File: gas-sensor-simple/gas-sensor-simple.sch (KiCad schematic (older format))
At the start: 43 parts, among them J1 RPi, J2 digital header, J3 digital header, J4 1x2, J5 1x2, J6 1x2, J7 1x2, U1 MQ-8, U10 RG LED, U12 LM393, U13 ads1x15, U14 ads1x15, U15 BME280, U2 MQ-4, U3 DFRobotCO2, U4 O2, U5 7407, U6 7407, U7 RG LED, U8 RG LED, U9 RG LED

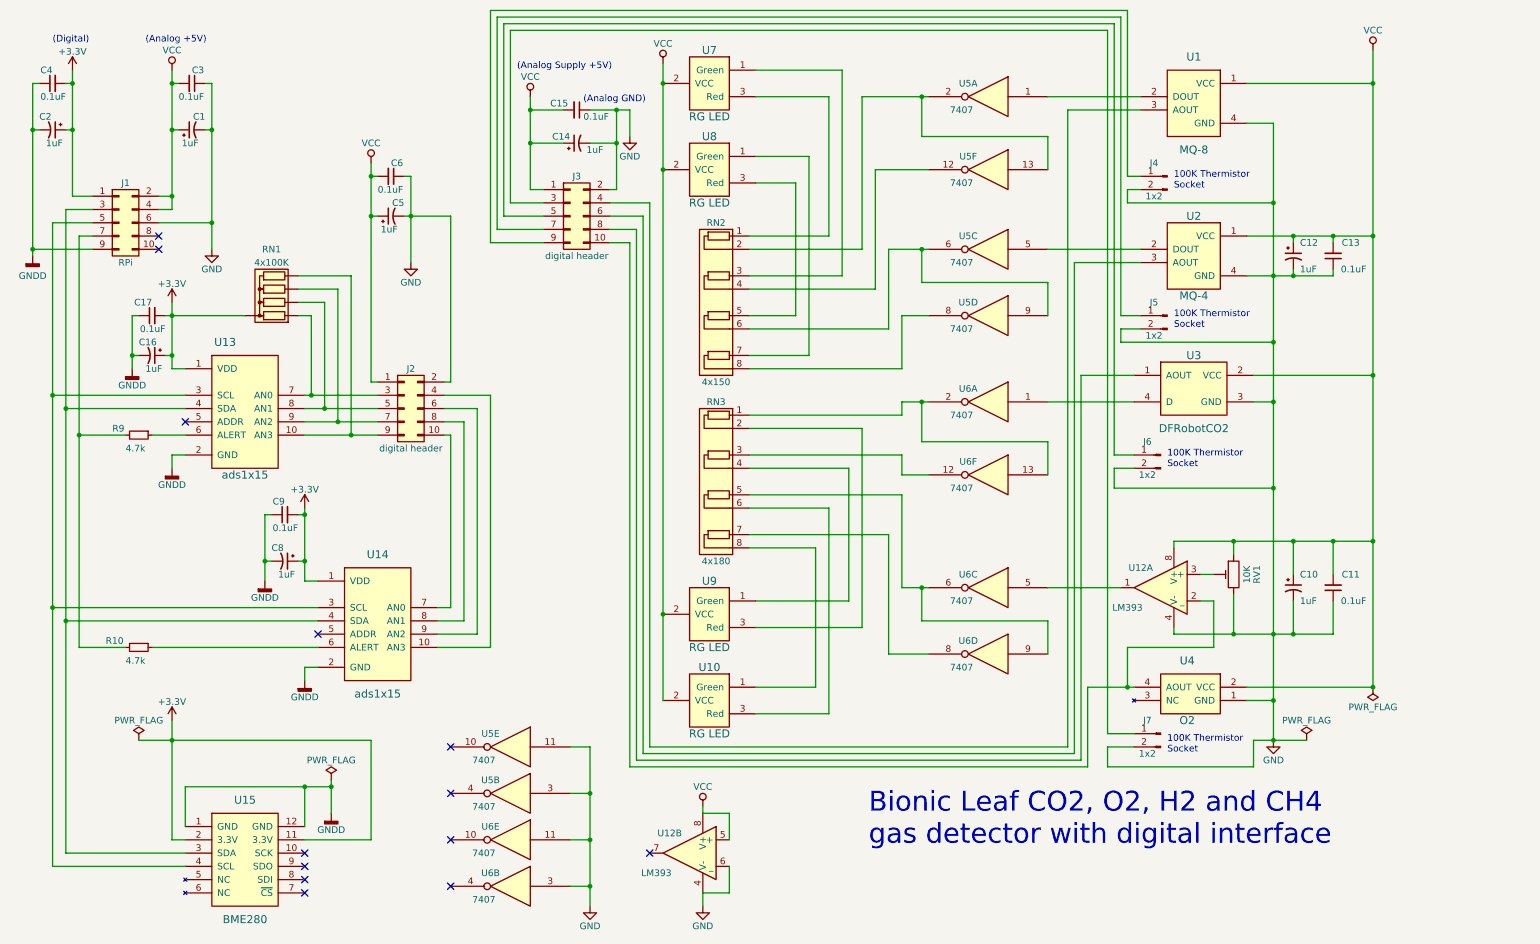
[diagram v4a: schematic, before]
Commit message: Add ground planes. Create new gerbers in layout2.gerbers.
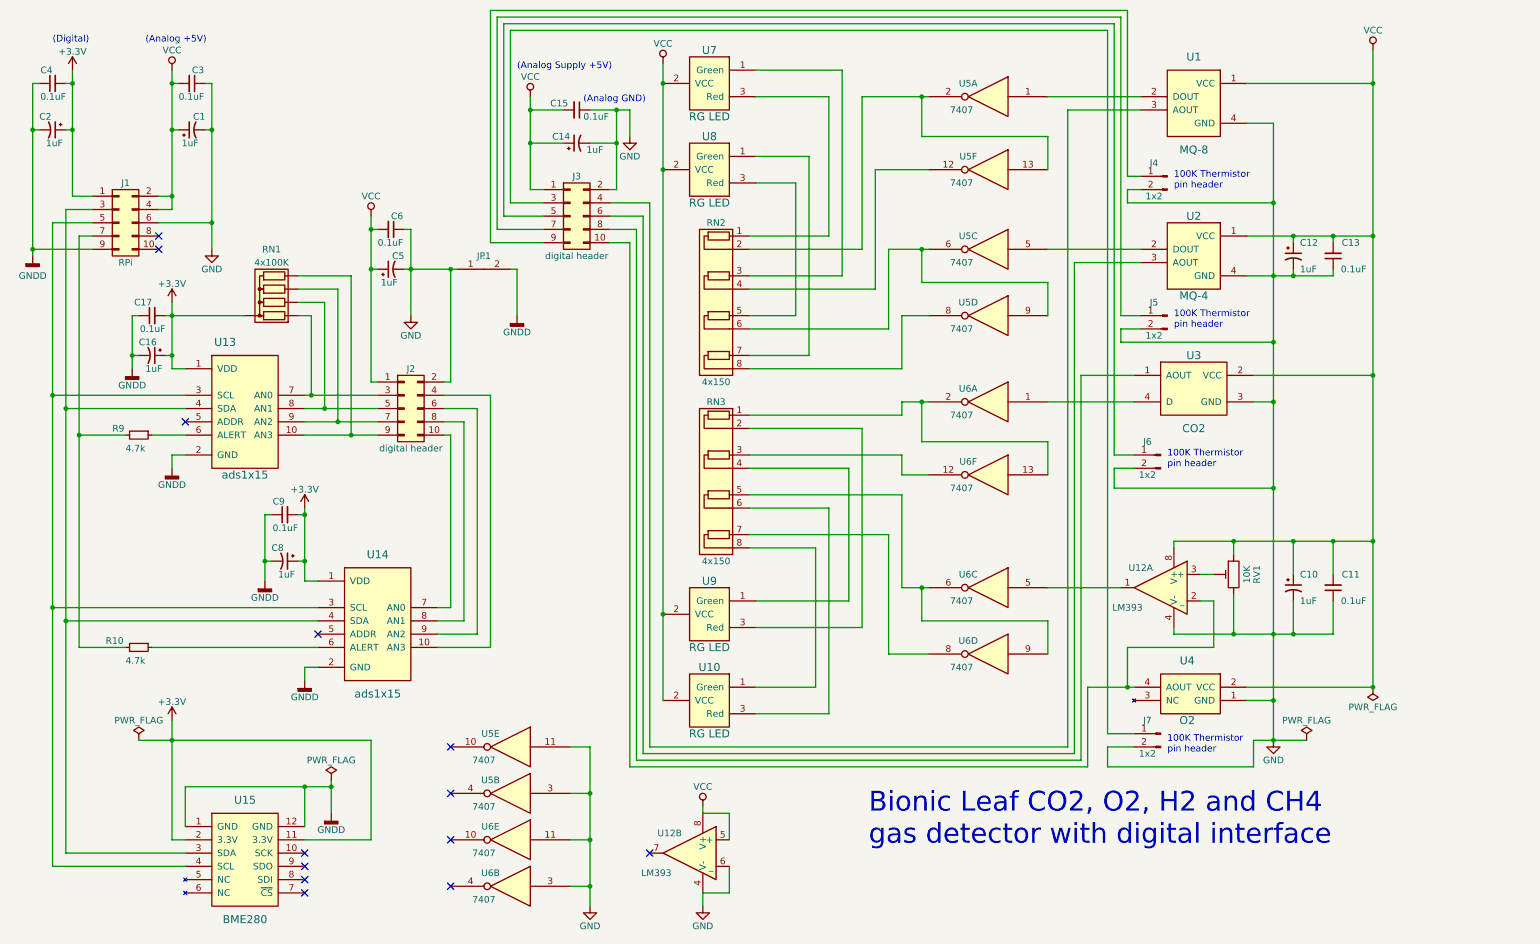
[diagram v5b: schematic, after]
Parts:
- added JP1: ., Resistors_SMD:R_0402_NoSilk, symbol pavillion
- RN3: value 4x180 -> 4x150
- U3: value DFRobotCO2 -> CO2
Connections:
- net GND: now also JP1.1
- net GNDD: now also JP1.2
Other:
- note added: "100K Thermistor\npin header"
- note removed: "100K Thermistor\nSocket"
- moved on the sheet: C5, C6
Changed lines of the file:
@@
 P 9500 3600
 F 0 "U3" H 9500 3850 60  0000 C CNN
-F 1 "DFRobotCO2" H 9500 3300 60  0000 C CNN
+F 1 "CO2" H 9500 3300 60  0000 C CNN
 F 2 "Socket_Strips:Socket_Strip_Straight_1x04_Pitch2.54mm" H 9500 3300 60  0001 C CNN
 F 3 "" H 9500 3300 60  0001 C CNN
@@
 L GND #PWR015
 U 1 1 5A065453
-P 3600 2650
-F 0 "#PWR015" H 3600 2400 50  0001 C CNN
-F 1 "GND" H 3600 2500 50  0000 C CNN
-F 2 "" H 3600 2650 50  0001 C CNN
-F 3 "" H 3600 2650 50  0001 C CNN
-	1    3600 2650
+P 3600 3050
+F 0 "#PWR015" H 3600 2800 50  0001 C CNN
+F 1 "GND" H 3600 2900 50  0000 C CNN
+F 2 "" H 3600 3050 50  0001 C CNN
+F 3 "" H 3600 3050 50  0001 C CNN
+	1    3600 3050
 	1    0    0    -1
 $EndComp
@@
 L VCC #PWR016
 U 1 1 5A024ADB
-P 3300 1900
-F 0 "#PWR016" H 3300 1750 50  0001 C CNN
-F 1 "VCC" H 3300 2050 50  0000 C CNN
-F 2 "" H 3300 1900 50  0001 C CNN
-F 3 "" H 3300 1900 50  0001 C CNN
-	1    3300 1900
+P 3300 2300
+F 0 "#PWR016" H 3300 2150 50  0001 C CNN
+F 1 "VCC" H 3300 2450 50  0000 C CNN
+F 2 "" H 3300 2300 50  0001 C CNN
+F 3 "" H 3300 2300 50  0001 C CNN
+	1    3300 2300
 	1    0    0    -1
 $EndComp
@@
 L CP1_Small C5
 U 1 1 5A0B3058
-P 3450 2300
-F 0 "C5" V 3550 2200 50  0000 L CNN
-F 1 "1uF" V 3350 2250 50  0000 L CNN
-F 2 "Capacitors_THT:CP_Radial_D5.0mm_P2.00mm" H 3450 2300 50  0001 C CNN
-F 3 "" H 3450 2300 50  0001 C CNN
-	1    3450 2300
+P 3450 2700
+F 0 "C5" V 3550 2600 50  0000 L CNN
+F 1 "1uF" V 3350 2650 50  0000 L CNN
+F 2 "Capacitors_THT:CP_Radial_D5.0mm_P2.00mm" H 3450 2700 50  0001 C CNN
+F 3 "" H 3450 2700 50  0001 C CNN
+	1    3450 2700
 	0    -1   -1   0
 $EndComp
@@
 L C_Small C6
 U 1 1 5A0B305E
-P 3450 2000
-F 0 "C6" V 3350 2000 50  0000 L CNN
-F 1 "0.1uF" V 3550 1900 50  0000 L CNN
-F 2 "Capacitors_THT:C_Disc_D5.0mm_W2.5mm_P2.50mm" H 3450 2000 50  0001 C CNN
-F 3 "" H 3450 2000 50  0001 C CNN
-	1    3450 2000
+P 3450 2400
+F 0 "C6" V 3350 2400 50  0000 L CNN
+F 1 "0.1uF" V 3550 2300 50  0000 L CNN
+F 2 "Capacitors_THT:C_Disc_D5.0mm_W2.5mm_P2.50mm" H 3450 2400 50  0001 C CNN
+F 3 "" H 3450 2400 50  0001 C CNN
+	1    3450 2400
 	0    1    1    0
 $EndComp
@@
 Wire Wire Line
 	9000 750  4200 750
-Wire Wire Line
-	3300 1900 3300 3550
-Connection ~ 3300 2300
-Connection ~ 3300 2000
+Connection ~ 3300 2700
+Connection ~ 3300 2400
 Wire Wire Line
 	4500 1400 4500 2100
@@
 	3850 3550 3900 3550
 Wire Wire Line
-	3550 2000 3600 2000
-Wire Wire Line
-	3600 2000 3600 2650
-Wire Wire Line
-	3550 2300 3900 2300
-Connection ~ 3600 2300
+	3550 2400 3600 2400
+Wire Wire Line
+	3600 2400 3600 3050
+Wire Wire Line
+	3550 2700 3950 2700
+Connection ~ 3600 2700
 Wire Wire Line
 	2750 4900 2800 4900
@@
 Wire Wire Line
 	1050 2150 1200 2150
-Wire Wire Line
-	3900 2300 3900 3550
 Wire Wire Line
 	1650 3950 1900 3950
@@
 $EndComp
 Text Notes 9350 2100 0    50   ~ 0
-100K Thermistor\nSocket
+100K Thermistor\npin header
 Wire Wire Line
 	8950 3050 9100 3050
@@
 $EndComp
 Text Notes 9350 3150 0    50   ~ 0
-100K Thermistor\nSocket
+100K Thermistor\npin header
 Wire Wire Line
 	8950 3150 8950 3250
@@
 $EndComp
 Text Notes 9300 4200 0    50   ~ 0
-100K Thermistor\nSocket
+100K Thermistor\npin header
 Wire Wire Line
 	9050 4200 8900 4200
@@
 $EndComp
 Text Notes 9300 6350 0    50   ~ 0
-100K Thermistor\nSocket
+100K Thermistor\npin header
 Wire Wire Line
 	8850 6450 9950 6450
@@
 $EndComp
 Wire Wire Line
-	3350 2000 3300 2000
-Wire Wire Line
-	3300 2300 3350 2300
+	3350 2400 3300 2400
+Wire Wire Line
+	3300 2700 3350 2700
 Wire Wire Line
 	2750 3050 2850 3050
@@
 P 5950 4300
 F 0 "RN3" V 5350 4350 50  0000 C CNN
-F 1 "4x180" V 6550 4350 50  0000 C CNN
+F 1 "4x150" V 6550 4350 50  0000 C CNN
 F 2 "Resistors_THT:R_Array_SIP8" V 6625 4300 50  0001 C CNN
 F 3 "" H 5950 4300 50  0001 C CNN
@@
 Wire Wire Line
 	3900 5250 3900 3950
+Wire Wire Line
+	3900 3550 3900 2700
+$Comp
+L GNDD #PWR027
+U 1 1 5A1E376D
+P 4400 3050
+F 0 "#PWR027" H 4400 2800 50  0001 C CNN
+F 1 "GNDD" H 4400 2925 50  0000 C CNN
+F 2 "" H 4400 3050 50  0001 C CNN
+F 3 "" H 4400 3050 50  0001 C CNN
+	1    4400 3050
+	1    0    0    -1
+$EndComp
+Wire Wire Line
+	4400 2700 4400 3050
+Connection ~ 3900 2700
+Wire Wire Line
+	4350 2700 4400 2700
+$Comp
+L pavillion JP1
+U 1 1 5A1F1560
+P 4150 2700
+F 0 "JP1" H 4150 2800 50  0000 C CNN
+F 1 "." H 4150 2800 50  0000 C CNN
+F 2 "Resistors_SMD:R_0402_NoSilk" H 4150 2700 150 0001 C CNN
+F 3 "" H 4150 2700 150 0001 C CNN
+	1    4150 2700
+	1    0    0    -1
+$EndComp
+Wire Wire Line
+	3300 2300 3300 3550
 $EndSCHEMATC
